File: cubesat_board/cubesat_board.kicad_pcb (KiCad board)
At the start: 2 copper layers, 91.4 x 91.4 mm, 3 parts, among them J1 CONN_02X26, J2 CONN_02X26

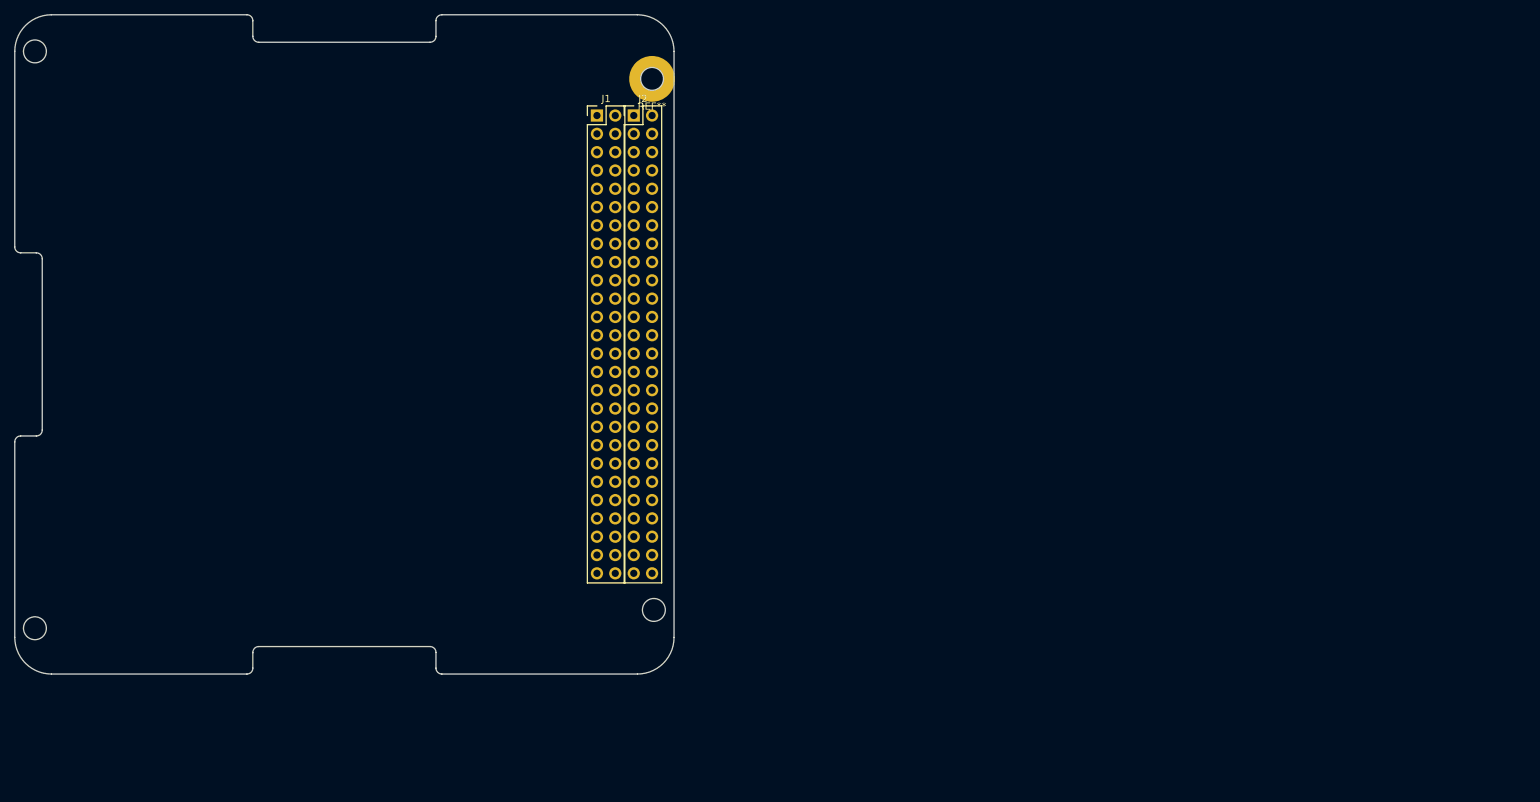
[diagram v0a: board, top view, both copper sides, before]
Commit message: Changed dimensions of the board to accommodate a wider spacing between the mounting holes and the PCB borders. Decreased width of wire slots. Re-created PCB template
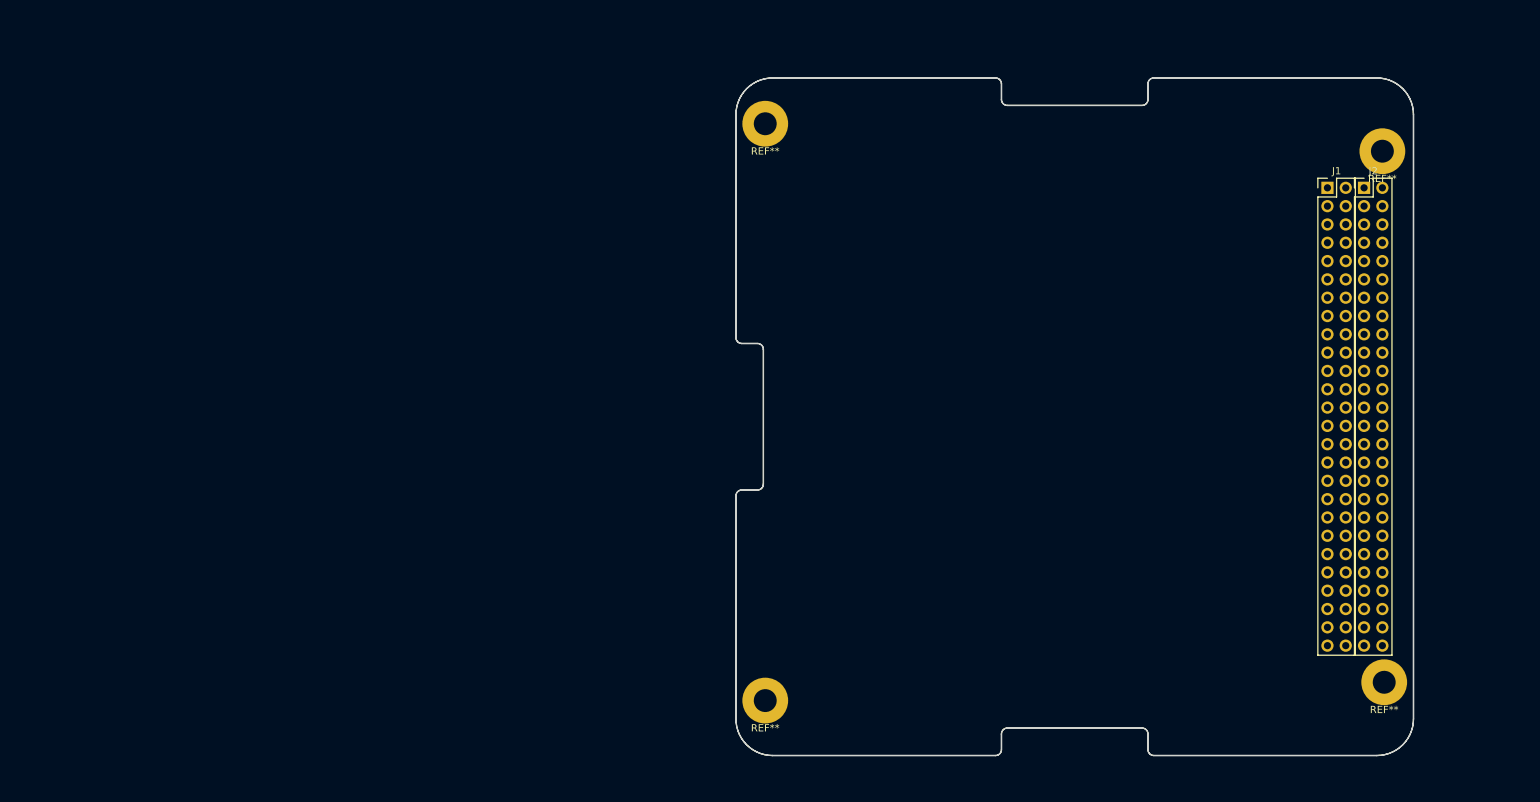
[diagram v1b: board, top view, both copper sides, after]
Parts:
- added REF**: 0.125in mounting hole, mounting_holes:0.125in_mounting_hole, F.Cu at (204.1, 106.9)
- added REF**: 0.125in mounting hole, mounting_holes:0.125in_mounting_hole, F.Cu at (118.2, 109.4)
- added REF**: 0.125in mounting hole, mounting_holes:0.125in_mounting_hole, F.Cu at (118.2, 29.4)
- moved J1 101.8 mm to (196.2, 38.3)
- moved J2 101.8 mm to (201.3, 38.3)
- moved REF** 101.8 mm to (203.8, 33.2)
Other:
- board size 91.4 x 91.4 mm -> 94 x 94 mm

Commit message: Finalized physical pcb template design, guidelines and rules to follow
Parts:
- moved J1 16.5 mm to (212.0, 43.4)
- moved J2 16.5 mm to (217.0, 43.4)
- moved REF** 16.5 mm to (219.6, 38.3)
- moved REF** 16.4 mm to (133.8, 114.5)
- moved REF** 16.4 mm to (133.8, 34.5)
- moved REF** 16.3 mm to (219.6, 112.0)
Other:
- outline, holes or cut-outs redrawn
- copper layers 2 -> 4
